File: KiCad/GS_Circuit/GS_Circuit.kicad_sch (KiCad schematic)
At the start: 13 parts, among them J1 AVR-ISP-6, SW1 SW_Push, SW2 SW_SPST, U2 ATtiny85V-10P

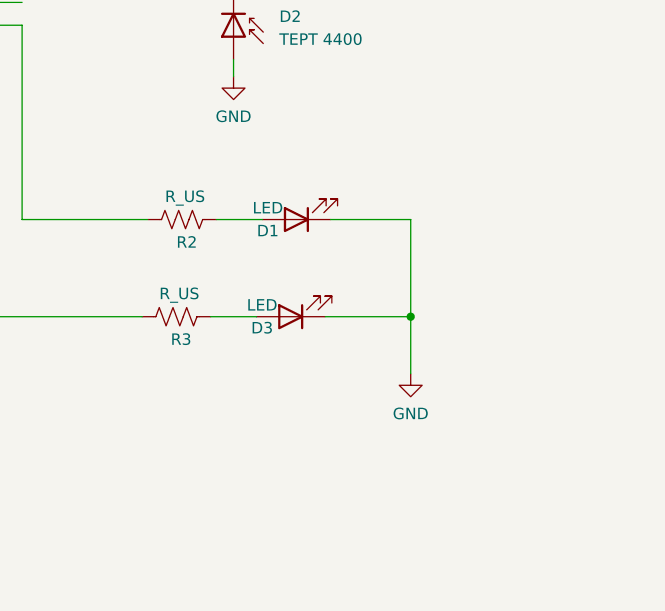
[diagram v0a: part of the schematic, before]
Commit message: Foot Print and Componentry
First Try at foot print.

LEDs are sourced
Need help on switches.
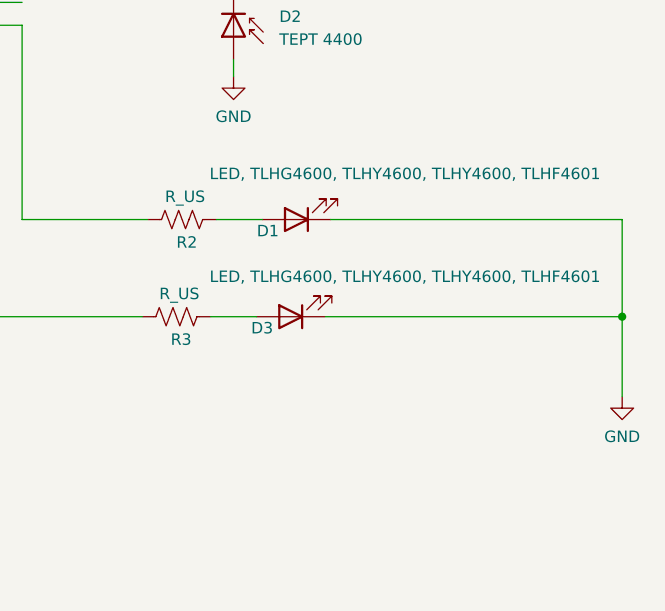
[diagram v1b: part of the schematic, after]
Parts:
- BT1: footprint (none) -> Battery:BatteryHolder_TruPower_BH-331P_3xAA
- C1: footprint (none) -> Capacitor_THT:C_Disc_D4.3mm_W1.9mm_P5.00mm
- D1, D3: value LED -> LED, TLHG4600, TLHY4600, TLHY4600, TLHF4601; footprint (none) -> LED_THT:LED_D3.0mm
- D2: footprint (none) -> Library:TEPT4400
- J1: footprint (none) -> Connector_IDC:IDC-Header_2x03_P2.54mm_Vertical
- R1, R2, R3, R4: footprint (none) -> Capacitor_SMD:C_1206_3216Metric
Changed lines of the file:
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@@
 	)
 	(junction
-		(at 151.13 90.805)
+		(at 174.625 90.805)
 		(diameter 0)
 		(color 0 0 0 0)
@@
 	(wire
 		(pts
-			(xy 151.13 80.01) (xy 151.13 90.805)
+			(xy 174.625 80.01) (xy 174.625 90.805)
 		)
 		(stroke
@@
 	(wire
 		(pts
-			(xy 141.605 90.805) (xy 151.13 90.805)
+			(xy 141.605 90.805) (xy 174.625 90.805)
 		)
 		(stroke
@@
 	(wire
 		(pts
-			(xy 142.24 80.01) (xy 151.13 80.01)
+			(xy 142.24 80.01) (xy 174.625 80.01)
 		)
 		(stroke
@@
 	(wire
 		(pts
-			(xy 151.13 97.155) (xy 151.13 90.805)
+			(xy 174.625 99.695) (xy 174.625 90.805)
 		)
 		(stroke
@@
 			)
 		)
-		(property "Footprint" ""
+		(property "Footprint" "Library:TEPT4400"
 			(at 131.445 58.42 0)
 			(effects
@@
 	(symbol
 		(lib_id "power:GND")
-		(at 151.13 97.155 0)
+		(at 174.625 99.695 0)
 		(unit 1)
 		(exclude_from_sim no)
@@
 		(fields_autoplaced yes)
 		(property "Reference" "#PWR010"
-			(at 151.13 103.505 0)
+			(at 174.625 106.045 0)
 			(effects
 				(font
@@
 		)
 		(property "Value" "GND"
-			(at 151.13 101.6 0)
+			(at 174.625 104.14 0)
 			(effects
 				(font
@@
 		)
 		(property "Footprint" ""
-			(at 151.13 97.155 0)
+			(at 174.625 99.695 0)
 			(effects
 				(font
@@
 		)
 		(property "Datasheet" ""
-			(at 151.13 97.155 0)
+			(at 174.625 99.695 0)
 			(effects
 				(font
@@
 		)
 		(property "Description" "Power symbol creates a global label with name \"GND\" , ground"
-			(at 151.13 97.155 0)
+			(at 174.625 99.695 0)
 			(effects
 				(font
@@
 			)
 		)
-		(property "Footprint" ""
+		(property "Footprint" "Capacitor_THT:C_Disc_D4.3mm_W1.9mm_P5.00mm"
 			(at 47.3202 44.45 0)
 			(effects
@@
 			)
 		)
-		(property "Value" "LED"
-			(at 134.62 89.535 0)
-			(effects
-				(font
-					(size 1.27 1.27)
-				)
-			)
-		)
-		(property "Footprint" ""
+		(property "Value" "LED, TLHG4600, TLHY4600, TLHY4600, TLHF4601"
+			(at 150.495 86.36 0)
+			(effects
+				(font
+					(size 1.27 1.27)
+				)
+			)
+		)
+		(property "Footprint" "LED_THT:LED_D3.0mm"
 			(at 137.795 90.805 0)
 			(effects
@@
 			)
 		)
-		(property "Footprint" ""
+		(property "Footprint" "Capacitor_SMD:C_1206_3216Metric"
 			(at 124.841 91.821 90)
 			(effects
@@
 			)
 		)
-		(property "Footprint" ""
+		(property "Footprint" "Capacitor_SMD:C_1206_3216Metric"
 			(at 125.476 81.026 90)
 			(effects
@@
 			)
 		)
-		(property "Footprint" ""
+		(property "Footprint" "Connector_IDC:IDC-Header_2x03_P2.54mm_Vertical"
 			(at 36.83 100.965 90)
 			(effects
@@
 			)
 		)
-		(property "Footprint" ""
+		(property "Footprint" "Capacitor_SMD:C_1206_3216Metric"
 			(at 132.461 47.879 90)
 			(effects
@@
 			)
 		)
-		(property "Value" "LED"
-			(at 135.255 78.74 0)
-			(effects
-				(font
-					(size 1.27 1.27)
-				)
-			)
-		)
-		(property "Footprint" ""
+		(property "Value" "LED, TLHG4600, TLHY4600, TLHY4600, TLHF4601"
+			(at 150.495 74.93 0)
+			(effects
+				(font
+					(size 1.27 1.27)
+				)
+			)
+		)
+		(property "Footprint" "LED_THT:LED_D3.0mm"
 			(at 138.43 80.01 0)
 			(effects
@@
 			)
 		)
-		(property "Footprint" ""
+		(property "Footprint" "Battery:BatteryHolder_TruPower_BH-331P_3xAA"
 			(at 29.845 55.626 90)
 			(effects
@@
 			)
 		)
-		(property "Footprint" ""
+		(property "Footprint" "Capacitor_SMD:C_1206_3216Metric"
 			(at 81.534 87.376 90)
 			(effects

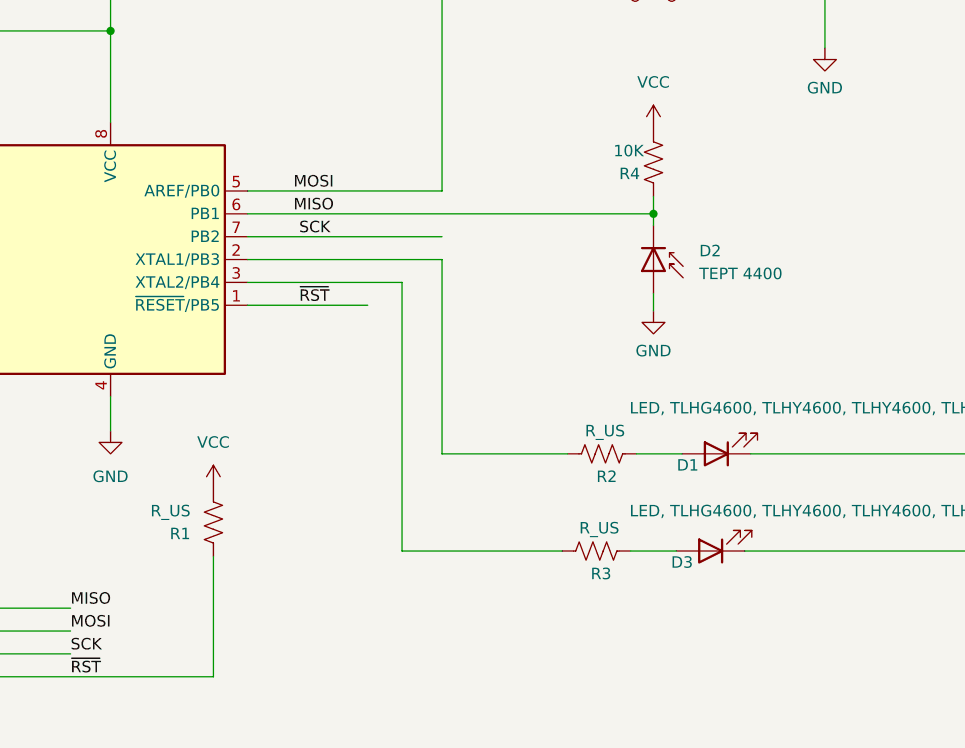
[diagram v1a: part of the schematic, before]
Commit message: First try foot print
Added library components with foot prints.  (photo sensor and switches).

First draft at PCB layout.
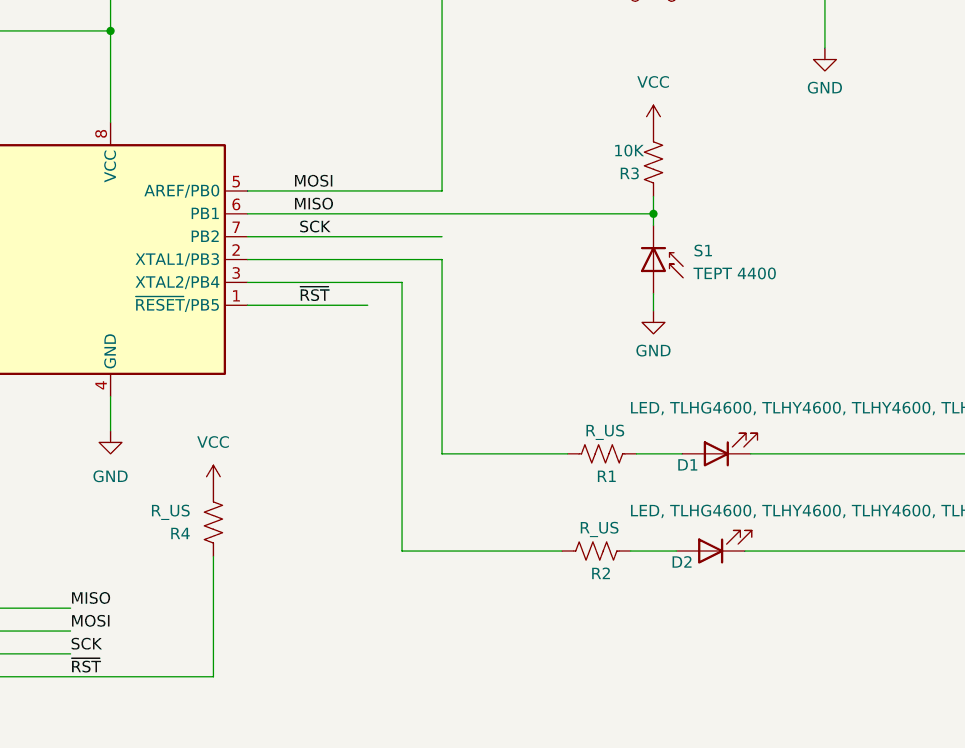
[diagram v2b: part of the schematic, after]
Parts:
- SW1, SW2: footprint (none) -> Library:LC 1258
- renumbered D3 to D2, R2 to R1, R3 to R2, R4 to R3, R1 to R4, D2 to S1
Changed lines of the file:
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@@
 		(dnp no)
 		(fields_autoplaced yes)
-		(property "Reference" "D2"
-			(at 136.525 57.4674 90)
+		(property "Reference" "S1"
+			(at 135.89 57.4674 90)
 			(effects
 				(font
@@
 		)
 		(property "Value" "TEPT 4400"
-			(at 136.525 60.0074 90)
+			(at 135.89 60.0074 90)
 			(effects
 				(font
@@
 			(project ""
 				(path "/9b478156-6fed-4cfd-9c5f-11981dbd0d2e"
-					(reference "D2")
+					(reference "S1")
 					(unit 1)
 				)
@@
 			)
 		)
-		(property "Footprint" ""
+		(property "Footprint" "Library:LC 1258"
 			(at 29.845 41.91 0)
 			(effects
@@
 			)
 		)
-		(property "Footprint" ""
+		(property "Footprint" "Library:LC 1258"
 			(at 131.445 24.13 0)
 			(effects
@@
 		(on_board yes)
 		(dnp no)
-		(property "Reference" "D3"
+		(property "Reference" "D2"
 			(at 134.62 92.075 0)
 			(effects
@@
 			(project "GS_Circuit"
 				(path "/9b478156-6fed-4cfd-9c5f-11981dbd0d2e"
-					(reference "D3")
+					(reference "D2")
 					(unit 1)
 				)
@@
 		(on_board yes)
 		(dnp no)
-		(property "Reference" "R3"
+		(property "Reference" "R2"
 			(at 124.46 93.345 90)
 			(effects
@@
 			(project "GS_Circuit"
 				(path "/9b478156-6fed-4cfd-9c5f-11981dbd0d2e"
-					(reference "R3")
+					(reference "R2")
 					(unit 1)
 				)
@@
 		(on_board yes)
 		(dnp no)
-		(property "Reference" "R2"
+		(property "Reference" "R1"
 			(at 125.095 82.55 90)
 			(effects
@@
 			(project ""
 				(path "/9b478156-6fed-4cfd-9c5f-11981dbd0d2e"
-					(reference "R2")
+					(reference "R1")
 					(unit 1)
 				)
@@
 		(on_board yes)
 		(dnp no)
-		(property "Reference" "R4"
+		(property "Reference" "R3"
 			(at 127.635 48.895 0)
 			(effects
@@
 			(project "GS_Circuit"
 				(path "/9b478156-6fed-4cfd-9c5f-11981dbd0d2e"
-					(reference "R4")
+					(reference "R3")
 					(unit 1)
 				)
@@
 		(on_board yes)
 		(dnp no)
-		(property "Reference" "R1"
+		(property "Reference" "R4"
 			(at 80.01 88.9001 0)
 			(effects
@@
 			(project "GS_Circuit"
 				(path "/9b478156-6fed-4cfd-9c5f-11981dbd0d2e"
-					(reference "R1")
-					(unit 1)
-				)
+					(reference "R4")
+					(unit 1)
+				)

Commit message: MD Electron Feedback 1
-Changed Library Structure
-Fixed switch footprint issue
-Added PCB over all footprint and layout
-Moved silkscreen labels
-
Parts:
- R1, R2, R3, R4: footprint Capacitor_SMD:C_1206_3216Metric -> Resistor_THT:R_Axial_DIN0207_L6.3mm_D2.5mm_P10.16mm_Horizontal
- S1: footprint Library:TEPT4400 -> GS_Parts:TEPT4400
- SW1, SW2: footprint Library:LC 1258 -> GS_Parts:LC 1258
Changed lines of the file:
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@@
 			)
 		)
-		(property "Footprint" "Library:TEPT4400"
+		(property "Footprint" "GS_Parts:TEPT4400"
 			(at 131.445 58.42 0)
 			(effects
@@
 			)
 		)
-		(property "Footprint" "Library:LC 1258"
+		(property "Footprint" "GS_Parts:LC 1258"
 			(at 29.845 41.91 0)
 			(effects
@@
 			)
 		)
-		(property "Footprint" "Library:LC 1258"
+		(property "Footprint" "GS_Parts:LC 1258"
 			(at 131.445 24.13 0)
 			(effects
@@
 			)
 		)
-		(property "Footprint" "Capacitor_SMD:C_1206_3216Metric"
+		(property "Footprint" "Resistor_THT:R_Axial_DIN0207_L6.3mm_D2.5mm_P10.16mm_Horizontal"
 			(at 124.841 91.821 90)
 			(effects
@@
 			)
 		)
-		(property "Footprint" "Capacitor_SMD:C_1206_3216Metric"
+		(property "Footprint" "Resistor_THT:R_Axial_DIN0207_L6.3mm_D2.5mm_P10.16mm_Horizontal"
 			(at 125.476 81.026 90)
 			(effects
@@
 			)
 		)
-		(property "Footprint" "Capacitor_SMD:C_1206_3216Metric"
+		(property "Footprint" "Resistor_THT:R_Axial_DIN0207_L6.3mm_D2.5mm_P10.16mm_Horizontal"
 			(at 132.461 47.879 90)
 			(effects
@@
 			)
 		)
-		(property "Footprint" "Capacitor_SMD:C_1206_3216Metric"
+		(property "Footprint" "Resistor_THT:R_Axial_DIN0207_L6.3mm_D2.5mm_P10.16mm_Horizontal"
 			(at 81.534 87.376 90)
 			(effects

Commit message: Fixed Battery Layout
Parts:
- BT1: footprint Battery:BatteryHolder_TruPower_BH-331P_3xAA -> GS_Parts:BatteryHolder_Keystone_2464
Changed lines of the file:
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@@
 			)
 		)
-		(property "Footprint" "Battery:BatteryHolder_TruPower_BH-331P_3xAA"
+		(property "Footprint" "GS_Parts:BatteryHolder_Keystone_2464"
 			(at 29.845 55.626 90)
 			(effects
